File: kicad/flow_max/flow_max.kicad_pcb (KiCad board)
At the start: 2 copper layers, 13 parts, among them U1 PAA3905E1, U10 PAT9136E1, U11 BMP390, U12 AFBR-S50LX85D, U13 SK9822-EC20, U14 LM66100DCKR, U2 MIC5504-1.8YMT, U3 MPM3811GG-Z, U4 ICM-45686, U6 VL53L1CXV0FY1, U7 IST8310, U8 TJA1462ATK, U9 TJA1103AHN

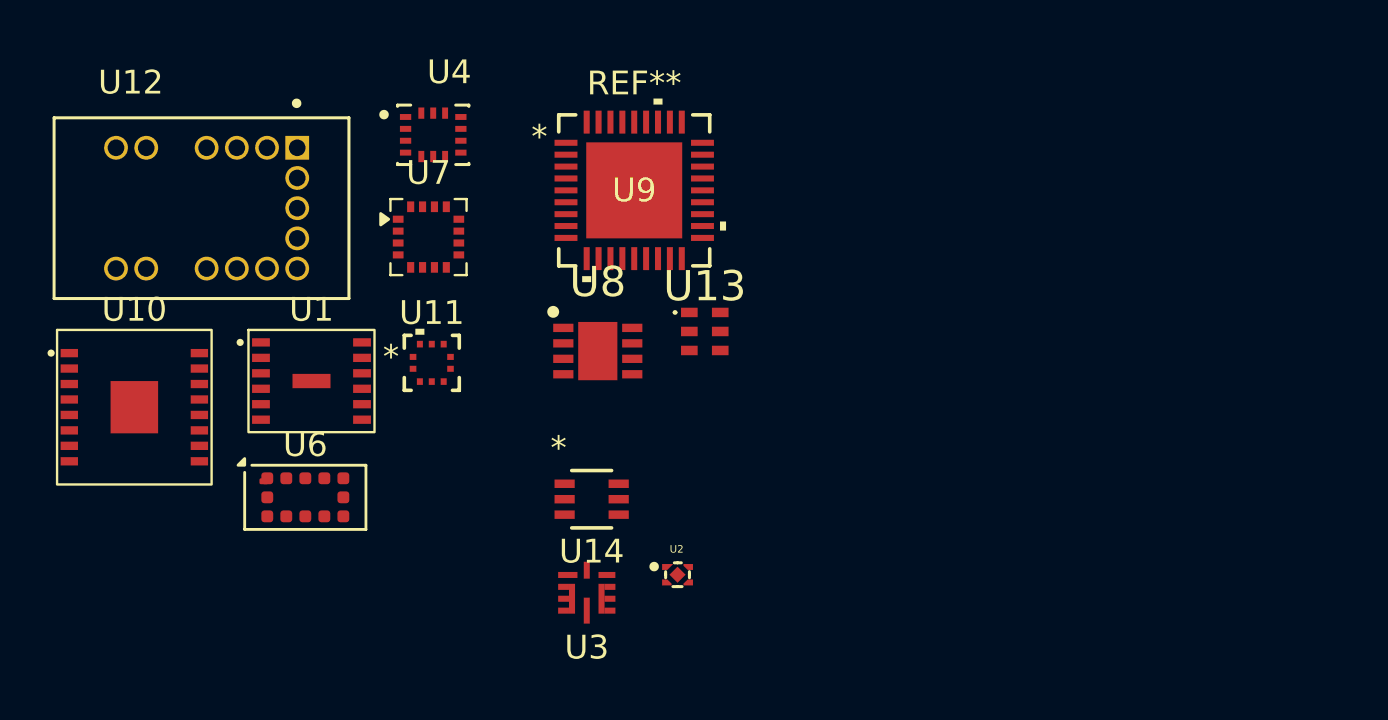
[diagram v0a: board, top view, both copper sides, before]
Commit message: Added in the schematic common mode choke filters and TVS diodes to parts where it is needed. Made the polarity protection circuit in schematic. Put placeholders for power supply regulators in schematic.
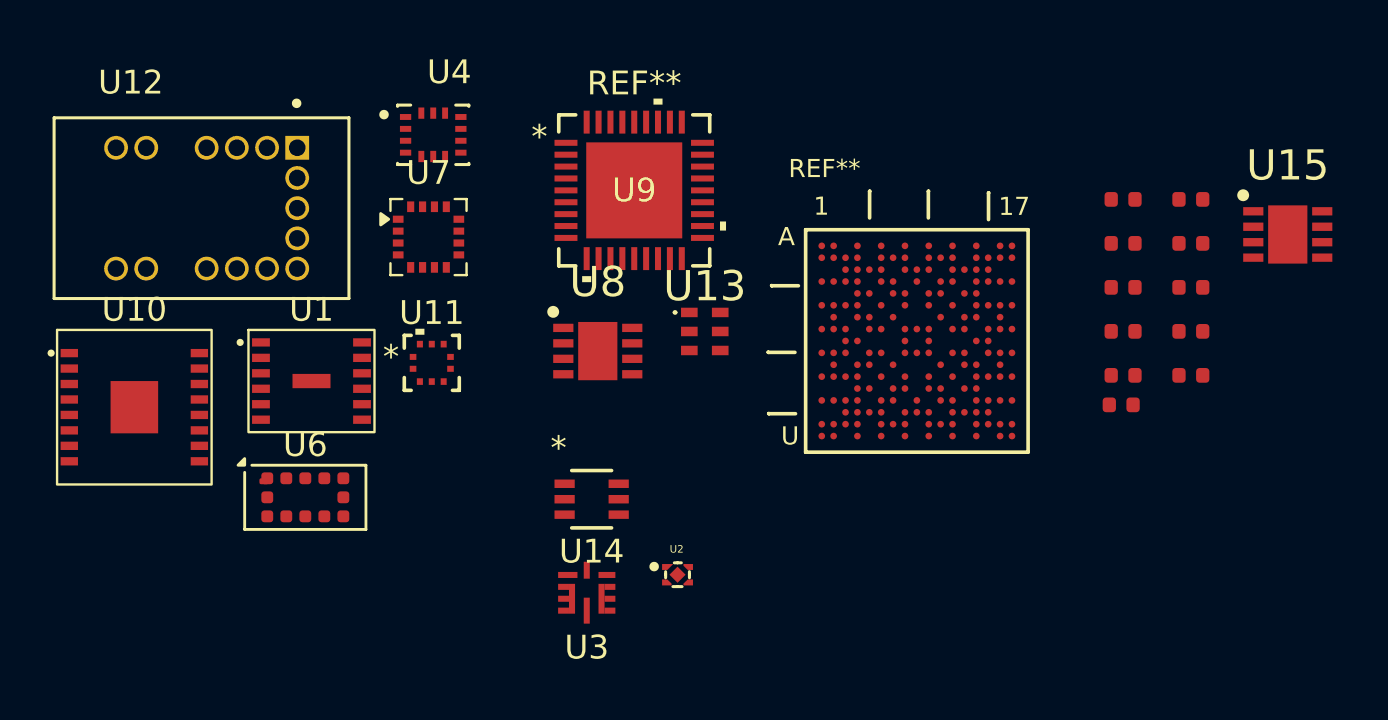
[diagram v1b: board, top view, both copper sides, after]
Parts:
- added C10: 1uF, PCM_JLCPCB:C_0402, F.Cu at (163.9, 86.8)
- added C11: 1uF, PCM_JLCPCB:C_0402, F.Cu at (163.9, 88.7)
- added C12: 100nF, PCM_JLCPCB:C_0402, F.Cu at (163.9, 90.5)
- added C13: 1uF, PCM_JLCPCB:C_0402, F.Cu at (163.9, 92.4)
- added C14: 100nF, PCM_JLCPCB:C_0402, F.Cu at (163.8, 93.6)
- added C15: 100nF, PCM_JLCPCB:C_0402, F.Cu at (166.7, 85.0)
- added C16: 10uF, PCM_JLCPCB:C_0402, F.Cu at (166.7, 86.8)
- added C17: 100nF, PCM_JLCPCB:C_0402, F.Cu at (166.7, 88.7)
- added C18: 100nF, PCM_JLCPCB:C_0402, F.Cu at (166.7, 90.5)
- added C19: 1uF, PCM_JLCPCB:C_0402, F.Cu at (166.7, 92.4)
- added C9: 100nF, PCM_JLCPCB:C_0402, F.Cu at (163.9, 85.0)
- added U15: TJA1462ATK, NXP_HV:SON65P300X300X100-9N-D, F.Cu at (170.8, 86.4)
- added U5: MCXN947VDFT, NXP_BGA:BGA184_0P5_9X9_SM, F.Cu at (155.2, 90.9)
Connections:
- U9 pad 1: unconnected-(U9-MDC-Pad1) -> /Communication/ENET0_MDC
- U9 pad 19: unconnected-(U9-RX_ER/GPIO2/TDO/CONFIG1-Pad19) -> /Communication/ENET0_RXER
- U9 pad 23: unconnected-(U9-RXD1/CONFIG4-Pad23) -> /Communication/ENET0_RXD1
- U9 pad 24: unconnected-(U9-RXD0/CONFIG5-Pad24) -> /Communication/ENET0_RXD0
- U9 pad 26: unconnected-(U9-RXC/GPIO8/TX_TCLK-Pad26) -> /Communication/ENET0_RXCLK
- U9 pad 28: unconnected-(U9-TX_ER/GPIO9/TCK-Pad28) -> /Communication/ENET0_TXER
- U9 pad 29: unconnected-(U9-TXC-Pad29) -> /Communication/ENET0_TXCLK
- U9 pad 3: unconnected-(U9-VDD_CORE-Pad3) -> Net-(U9-VDD_CORE)
- U9 pad 31: unconnected-(U9-TXD0-Pad31) -> /Communication/ENET0_TXD0
- U9 pad 32: unconnected-(U9-TXD1-Pad32) -> /Communication/ENET0_TXD1
- U9 pad 36: unconnected-(U9-MDIO-Pad36) -> /Communication/ENET0_MDIO
- U9 pad 37: unconnected-(U9-PAD-Pad37) -> GND
- U9 pad 4: unconnected-(U9-VREGD_IN-Pad4) -> VDDIO
- U9 pad 7: unconnected-(U9-VREGA_IN-Pad7) -> Net-(U9-VDDA_AO)
- U9 pad 8: unconnected-(U9-VREGA_OUT-Pad8) -> VDDA_TRX
- U9 pad 9: unconnected-(U9-VDDA_AO-Pad9) -> Net-(U9-VDDA_AO)
